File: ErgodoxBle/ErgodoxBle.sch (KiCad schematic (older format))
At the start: 90 parts, among them SW0:10 SW0:3, SW0:11 SW0:2, SW0:12 SW0:1, SW0:7 SW0:6, SW0:8 SW0:5, SW0:9 SW0:4, SW1:10 SW1:3, SW1:11 SW1:2, SW1:12 SW1:1, SW1:13 SW1:0, SW1:9 SW1:4, SW2:10 SW2:3, SW2:11 SW2:2, SW2:12 SW2:1, SW2:13 SW2:0, SW2:7 SW2:6, SW2:8 SW2:5, SW2:9 SW2:4, SW3:10 SW3:3, SW3:11 SW3:2, SW3:12 SW3:1, SW3:13 SW3:0, SW3:8 SW3:5, SW3:9 SW3:4, SW4:10 SW4:3, SW4:11 SW4:2, SW4:12 SW4:1, SW4:13 SW4:0, SW4:7 SW4:6, SW4:8 SW4:5, SW4:9 SW4:4, SW5:10 SW5:3, SW5:11 SW5:2, SW5:12 SW5:1, SW5:13 SW5:0, SW5:7 SW5:6, SW5:8 SW5:5, SW5:9 SW5:4

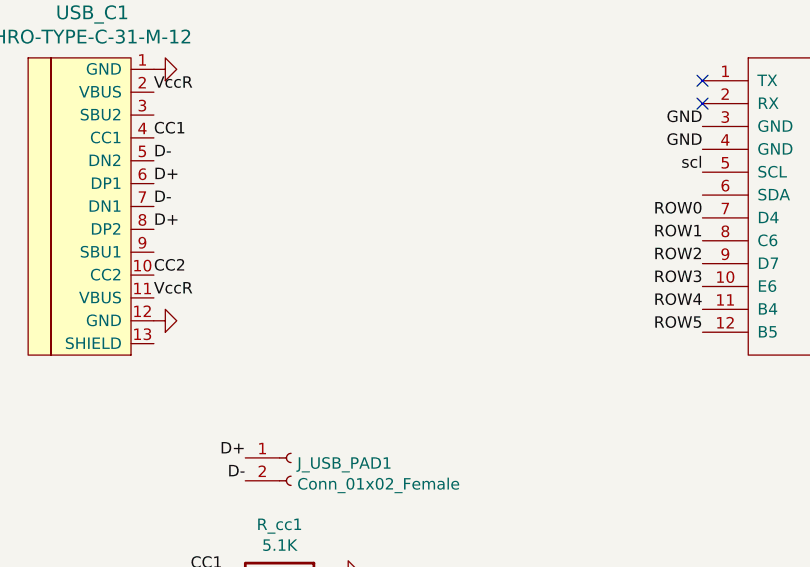
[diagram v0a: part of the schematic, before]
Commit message: Added pad for CR2032 module for bluemicro
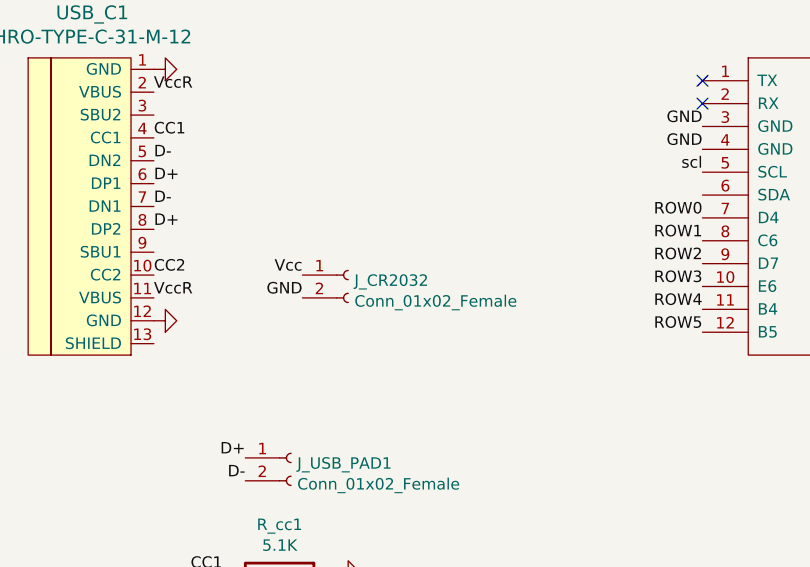
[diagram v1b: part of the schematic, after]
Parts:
- added J_CR2032: Conn_01x02_Female, Connector_Wire:SolderWirePad_1x02_P3.81mm_Drill0.8mm, symbol Connector:Conn_01x02_Female
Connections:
- net GND: now also J_CR2032.2 (Pin_2)
- net Vcc: now also J_CR2032.1 (Pin_1)
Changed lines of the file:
@@
 	1    0    0    -1
 $EndComp
+$Comp
+L Connector:Conn_01x02_Female J_CR2032
+U 1 1 5CA168E4
+P 2200 3200
+F 0 "J_CR2032" H 2227 3176 50  0000 L CNN
+F 1 "Conn_01x02_Female" H 2227 3085 50  0000 L CNN
+F 2 "Connector_Wire:SolderWirePad_1x02_P3.81mm_Drill0.8mm" H 2200 3200 50  0001 C CNN
+F 3 "~" H 2200 3200 50  0001 C CNN
+	1    2200 3200
+	1    0    0    -1
+$EndComp
+Text Label 2000 3200 2    50   ~ 0
+Vcc
+Text Label 2000 3300 2    50   ~ 0
+GND
 $EndSCHEMATC

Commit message: v 1.3, almost the final version
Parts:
- removed J_USB_PAD1: Conn_01x02_Female, Connector_Wire:SolderWirePad_1x02_P3.81mm_Drill0.8mm, symbol Connector:Conn_01x02_Female
- removed U_VR_IC1: AMS1117-3.3, Package_TO_SOT_SMD:SOT-223-3_TabPin2, symbol Regulator_Linear:AMS1117-3.3
- added D_RAW1, D_USB_HEADER1: D, Keebio-Parts:Diode-dual, symbol keyboard_parts:D
- added J_usb_break1: Conn_01x04_Female, Connector_Wire:SolderWirePad_1x04_P3.81mm_Drill1mm, symbol Connector:Conn_01x04_Female
- added U_ESD1: USBLC6-2SC6, Package_TO_SOT_SMD:SOT-23-6, symbol Power_Protection:USBLC6-2SC6
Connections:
- net D+: now also J_usb_break1.2 (Pin_2), U_ESD1.1 (IO1); no longer USB_C1.6 (DP1), USB_C1.8 (DP2)
- net D-: now also J_usb_break1.3 (Pin_3), U_ESD1.3 (IO2); no longer USB_C1.5 (DN2), USB_C1.7 (DN1)
- net GND: now also U_ESD1.2 (GND); no longer USB_C1.1 (GND), USB_C1.12 (GND), proMicro1.23 (GND)
- net VccR: now also D_RAW1.2, D_USB_HEADER1.2, U_ESD1.5 (VBUS)
- net VccRaw: now reaches proMicro1.24 (RAW)
- net VccRaw: now also D_RAW1.1
- new net D_IN+: USB_C1.6 (DP1), USB_C1.8 (DP2), U_ESD1.6 (IO1)
- new net D_IN-: USB_C1.5 (DN2), USB_C1.7 (DN1), U_ESD1.4 (IO2)
- new net GND_USB: J_usb_break1.4 (Pin_4), USB_C1.1 (GND), USB_C1.12 (GND), proMicro1.23 (GND)
- new net VUSB: D_USB_HEADER1.1, J_usb_break1.1 (Pin_1)
- no-connect marks 4 -> 3
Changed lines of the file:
@@
 	1    0    0    -1
 $EndComp
-$Comp
-L Connector:Conn_01x02_Female J_USB_PAD1
-U 1 1 5C943493
-P 1950 4000
-F 0 "J_USB_PAD1" H 1977 3976 50  0000 L CNN
-F 1 "Conn_01x02_Female" H 1977 3885 50  0000 L CNN
-F 2 "Connector_Wire:SolderWirePad_1x02_P3.81mm_Drill0.8mm" H 1950 4000 50  0001 C CNN
-F 3 "~" H 1950 4000 50  0001 C CNN
-	1    1950 4000
-	1    0    0    -1
-$EndComp
-Text Label 1750 4000 2    50   ~ 0
+Text Label 3300 4000 2    50   ~ 0
 D+
-Text Label 1750 4100 2    50   ~ 0
+Text Label 3300 4100 2    50   ~ 0
 D-
 $Comp
@@
 	0    -1   -1   0
 $EndComp
-Text Label 5150 2650 0    50   ~ 0
-Vcc
 Text Label 5150 2450 0    50   ~ 0
-GND
+GND_USB
 Text Label 3750 2550 2    50   ~ 0
 GND
@@
 NoConn ~ 3750 2350
 NoConn ~ 3750 2450
-NoConn ~ 5150 2350
 NoConn ~ 5150 2550
 $Comp
@@
 	1    0    0    -1
 $EndComp
-$Comp
-L component:GND #PWR0103
-U 1 1 5C6354D1
-P 1400 2300
-F 0 "#PWR0103" H 1400 2300 30  0001 C CNN
-F 1 "GND" H 1400 2230 30  0001 C CNN
-F 2 "" H 1400 2300 50  0001 C CNN
-F 3 "" H 1400 2300 50  0001 C CNN
-	1    1400 2300
-	0    -1   -1   0
-$EndComp
 Text Label 1350 2400 0    50   ~ 0
 VccR
@@
 Text Label 1350 3200 0    50   ~ 0
 CC2
-$Comp
-L component:GND #PWR0104
-U 1 1 5C646282
-P 1400 3400
-F 0 "#PWR0104" H 1400 3400 30  0001 C CNN
-F 1 "GND" H 1400 3330 30  0001 C CNN
-F 2 "" H 1400 3400 50  0001 C CNN
-F 3 "" H 1400 3400 50  0001 C CNN
-	1    1400 3400
-	0    -1   -1   0
-$EndComp
 Text Label 1350 3300 0    50   ~ 0
 VccR
 Text Label 1350 2700 0    50   ~ 0
-D-
+D_IN-
 Text Label 1350 2800 0    50   ~ 0
-D+
+D_IN+
 Text Label 1350 2900 0    50   ~ 0
-D-
+D_IN-
 Text Label 1350 3000 0    50   ~ 0
-D+
-$Comp
-L Regulator_Linear:AMS1117-3.3 U_VR_IC1
-U 1 1 5C499923
-P 2050 1400
-F 0 "U_VR_IC1" H 2050 1642 50  0000 C CNN
-F 1 "AMS1117-3.3" H 2050 1551 50  0000 C CNN
-F 2 "Package_TO_SOT_SMD:SOT-223-3_TabPin2" H 2050 1600 50  0001 C CNN
-F 3 "http://www.advanced-monolithic.com/pdf/ds1117.pdf" H 2150 1150 50  0001 C CNN
-	1    2050 1400
-	1    0    0    -1
-$EndComp
-Text Label 1750 1400 2    50   ~ 0
-VccR
-Text Label 2350 1400 0    50   ~ 0
-Vcc
-$Comp
-L component:GND #PWR0105
-U 1 1 5C49AE71
-P 2050 1750
-F 0 "#PWR0105" H 2050 1750 30  0001 C CNN
-F 1 "GND" H 2050 1680 30  0001 C CNN
-F 2 "" H 2050 1750 50  0001 C CNN
-F 3 "" H 2050 1750 50  0001 C CNN
-	1    2050 1750
-	1    0    0    -1
-$EndComp
+D_IN+
 $Comp
 L Connector:Conn_01x02_Female J_CR2032
@@
 Text Label 2000 3300 2    50   ~ 0
 GND
+$Comp
+L keyboard_parts:D D_RAW1
+U 1 1 5CBC3CF1
+P 2100 1250
+F 0 "D_RAW1" V 1919 1200 60  0000 C CNN
+F 1 "D" V 2250 1200 60  0001 C CNN
+F 2 "Keebio-Parts:Diode-dual" H 2100 1250 60  0001 C CNN
+F 3 "" H 2100 1250 60  0000 C CNN
+	1    2100 1250
+	0    1    1    0
+$EndComp
+$Comp
+L keyboard_parts:D D_USB_HEADER1
+U 1 1 5CBC3EC6
+P 2100 1600
+F 0 "D_USB_HEADER1" V 1919 1550 60  0000 C CNN
+F 1 "D" V 2250 1550 60  0001 C CNN
+F 2 "Keebio-Parts:Diode-dual" H 2100 1600 60  0001 C CNN
+F 3 "" H 2100 1600 60  0000 C CNN
+	1    2100 1600
+	0    1    1    0
+$EndComp
+Text Label 1950 1250 2    50   ~ 0
+VccR
+Text Label 1950 1600 2    50   ~ 0
+VccR
+Text Label 2150 1250 0    50   ~ 0
+VccRaw
+Text Label 2150 1600 0    50   ~ 0
+VUSB
+Text Label 5150 2350 0    50   ~ 0
+VccRaw
+Text Label 1350 2300 0    50   ~ 0
+GND_USB
+Text Label 1350 3400 0    50   ~ 0
+GND_USB
+Text Label 3300 3900 2    50   ~ 0
+VUSB
+Text Label 3300 4200 2    50   ~ 0
+GND_USB
+Text Label 5150 2650 0    50   ~ 0
+Vcc
+$Comp
+L Power_Protection:USBLC6-2SC6 U_ESD1
+U 1 1 5CBD2D52
+P 3450 1450
+F 0 "U_ESD1" H 3450 2128 50  0000 C CNN
+F 1 "USBLC6-2SC6" H 3450 2037 50  0000 C CNN
+F 2 "Package_TO_SOT_SMD:SOT-23-6" H 2700 1850 50  0001 C CNN
+F 3 "http://www2.st.com/resource/en/datasheet/CD00050750.pdf" H 3650 1800 50  0001 C CNN
+	1    3450 1450
+	1    0    0    -1
+$EndComp
+Text Label 3450 950  0    50   ~ 0
+VccR
+Text Label 2950 1350 2    50   ~ 0
+D_IN+
+Text Label 3950 1350 0    50   ~ 0
+D_IN-
+Text Label 2950 1550 2    50   ~ 0
+D+
+Text Label 3950 1550 0    50   ~ 0
+D-
+$Comp
+L component:GND #PWR0103
+U 1 1 5CBD3635
+P 3450 2000
+F 0 "#PWR0103" H 3450 2000 30  0001 C CNN
+F 1 "GND" H 3450 1930 30  0001 C CNN
+F 2 "" H 3450 2000 50  0001 C CNN
+F 3 "" H 3450 2000 50  0001 C CNN
+	1    3450 2000
+	1    0    0    -1
+$EndComp
+$Comp
+L Connector:Conn_01x04_Female J_usb_break1
+U 1 1 5CC50D9F
+P 3500 4000
+F 0 "J_usb_break1" H 3527 3976 50  0000 L CNN
+F 1 "Conn_01x04_Female" H 3527 3885 50  0000 L CNN
+F 2 "Connector_Wire:SolderWirePad_1x04_P3.81mm_Drill1mm" H 3500 4000 50  0001 C CNN
+F 3 "~" H 3500 4000 50  0001 C CNN
+	1    3500 4000
+	1    0    0    -1
+$EndComp
 $EndSCHEMATC

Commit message: final version before hardware testing
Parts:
- added USB_C2: HRO-TYPE-C-31-M-12, usbc_footprint:HRO-TYPE-C-31-M-12, symbol Type-C:HRO-TYPE-C-31-M-12
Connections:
- net CC1: now also USB_C2.4 (CC1)
- net CC2: now also USB_C2.10 (CC2)
- net D_IN+: now also USB_C2.6 (DP1), USB_C2.8 (DP2)
- net D_IN-: now also USB_C2.5 (DN2), USB_C2.7 (DN1)
- net GND_USB: now also USB_C2.1 (GND), USB_C2.12 (GND)
- net VccR: now also USB_C2.11 (VBUS), USB_C2.2 (VBUS)
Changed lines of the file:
@@
 	1    0    0    -1
 $EndComp
+$Comp
+L Type-C:HRO-TYPE-C-31-M-12 USB_C2
+U 1 1 5CC80FFB
+P 6450 1700
+F 0 "USB_C2" H 6281 2497 60  0000 C CNN
+F 1 "HRO-TYPE-C-31-M-12" H 6281 2391 60  0000 C CNN
+F 2 "usbc_footprint:HRO-TYPE-C-31-M-12" H 6450 1700 60  0001 C CNN
+F 3 "" H 6450 1700 60  0001 C CNN
+	1    6450 1700
+	1    0    0    -1
+$EndComp
+Text Label 6550 1250 0    50   ~ 0
+VccR
+Text Label 6550 1450 0    50   ~ 0
+CC1
+Text Label 6550 2050 0    50   ~ 0
+CC2
+Text Label 6550 2150 0    50   ~ 0
+VccR
+Text Label 6550 1550 0    50   ~ 0
+D_IN-
+Text Label 6550 1650 0    50   ~ 0
+D_IN+
+Text Label 6550 1750 0    50   ~ 0
+D_IN-
+Text Label 6550 1850 0    50   ~ 0
+D_IN+
+Text Label 6550 1150 0    50   ~ 0
+GND_USB
+Text Label 6550 2250 0    50   ~ 0
+GND_USB
 $EndSCHEMATC

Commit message: minor changes
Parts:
- removed D_RAW1, D_USB_HEADER1: D, Keebio-Parts:Diode-dual, symbol keyboard_parts:D
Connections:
- net VccR is gone; now on net VUSB: USB_C1.11 (VBUS), USB_C1.2 (VBUS), USB_C2.11 (VBUS), USB_C2.2 (VBUS), U_ESD1.5 (VBUS)
- net GND_USB: no longer proMicro1.23 (GND)
- net VccRaw: no longer names the net of proMicro1.24 (RAW)
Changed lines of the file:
@@
 	0    -1   -1   0
 $EndComp
-Text Label 5150 2450 0    50   ~ 0
-GND_USB
 Text Label 3750 2550 2    50   ~ 0
 GND
@@
 $EndComp
 Text Label 1350 2400 0    50   ~ 0
-VccR
+VUSB
 Text Label 1350 2600 0    50   ~ 0
 CC1
@@
 CC2
 Text Label 1350 3300 0    50   ~ 0
-VccR
+VUSB
 Text Label 1350 2700 0    50   ~ 0
 D_IN-
@@
 Text Label 2000 3300 2    50   ~ 0
 GND
-$Comp
-L keyboard_parts:D D_RAW1
-U 1 1 5CBC3CF1
-P 2100 1250
-F 0 "D_RAW1" V 1919 1200 60  0000 C CNN
-F 1 "D" V 2250 1200 60  0001 C CNN
-F 2 "Keebio-Parts:Diode-dual" H 2100 1250 60  0001 C CNN
-F 3 "" H 2100 1250 60  0000 C CNN
-	1    2100 1250
-	0    1    1    0
-$EndComp
-$Comp
-L keyboard_parts:D D_USB_HEADER1
-U 1 1 5CBC3EC6
-P 2100 1600
-F 0 "D_USB_HEADER1" V 1919 1550 60  0000 C CNN
-F 1 "D" V 2250 1550 60  0001 C CNN
-F 2 "Keebio-Parts:Diode-dual" H 2100 1600 60  0001 C CNN
-F 3 "" H 2100 1600 60  0000 C CNN
-	1    2100 1600
-	0    1    1    0
-$EndComp
-Text Label 1950 1250 2    50   ~ 0
-VccR
-Text Label 1950 1600 2    50   ~ 0
-VccR
-Text Label 2150 1250 0    50   ~ 0
-VccRaw
-Text Label 2150 1600 0    50   ~ 0
-VUSB
-Text Label 5150 2350 0    50   ~ 0
-VccRaw
 Text Label 1350 2300 0    50   ~ 0
 GND_USB
@@
 $EndComp
 Text Label 3450 950  0    50   ~ 0
-VccR
+VUSB
 Text Label 2950 1350 2    50   ~ 0
 D_IN+
@@
 $EndComp
 Text Label 6550 1250 0    50   ~ 0
-VccR
+VUSB
 Text Label 6550 1450 0    50   ~ 0
 CC1
@@
 CC2
 Text Label 6550 2150 0    50   ~ 0
-VccR
+VUSB
 Text Label 6550 1550 0    50   ~ 0
 D_IN-

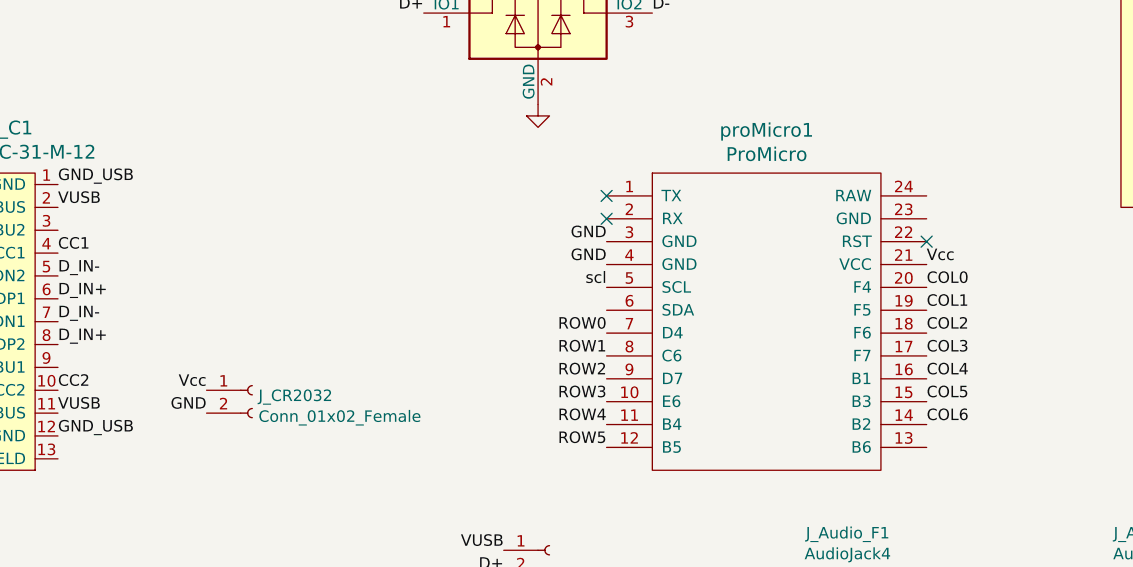
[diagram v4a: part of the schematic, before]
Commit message: added svg for case
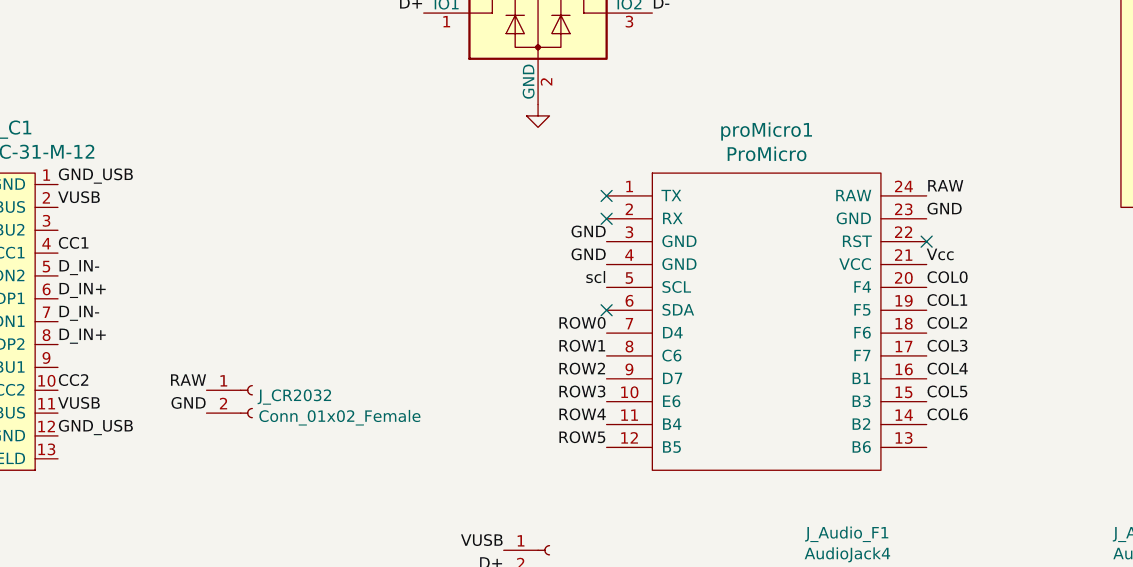
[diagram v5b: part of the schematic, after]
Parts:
- J_CR2032: footprint Connector_Wire:SolderWirePad_1x02_P3.81mm_Drill0.8mm -> usbc_footprint:Custom_SolderWirePad_1x02_P1.75mm_Drill1.09mm
- J_usb_break1: footprint Connector_Wire:SolderWirePad_1x04_P3.81mm_Drill1mm -> usbc_footprint:Custom_SolderWirePad_1x04_P1.7526mm_Drill1.0922mm
- SW0:10, SW0:11: footprint Keebio-Parts:Hybrid_PCB_100H_Dual_hole -> Keebio-Parts:Hybrid_PCB_200H-dual
- SW2:13, SW3:13, SW4:13, SW5:13: footprint Keebio-Parts:Hybrid_PCB_100H_Dual_hole -> usbc_footprint:correct_Hybrid_PCB_100v_150H_Dual_hole
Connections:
- net GND: now also proMicro1.23 (GND)
- net Vcc: no longer J_CR2032.1 (Pin_1)
- net RAW: now reaches proMicro1.24 (RAW)
- net RAW: now also J_CR2032.1 (Pin_1)
- no-connect marks 3 -> 4
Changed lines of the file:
@@
 F 0 "SW0:11" H 4850 9410 50  0000 C CNN
 F 1 "SW0:2" H 4700 9220 50  0000 C CNN
-F 2 "Keebio-Parts:Hybrid_PCB_100H_Dual_hole" H 4700 9300 60  0001 C CNN
+F 2 "Keebio-Parts:Hybrid_PCB_200H-dual" H 4700 9300 60  0001 C CNN
 F 3 "" H 4700 9300 60  0001 C CNN
 	1    4700 9300
@@
 F 0 "SW2:13" H 6250 8110 50  0000 C CNN
 F 1 "SW2:0" H 6100 7920 50  0000 C CNN
-F 2 "Keebio-Parts:Hybrid_PCB_100H_Dual_hole" H 6100 8000 60  0001 C CNN
+F 2 "usbc_footprint:correct_Hybrid_PCB_100v_150H_Dual_hole" H 6100 8000 60  0001 C CNN
 F 3 "" H 6100 8000 60  0001 C CNN
 	1    6100 8000
@@
 F 0 "SW3:13" H 6250 7460 50  0000 C CNN
 F 1 "SW3:0" H 6100 7270 50  0000 C CNN
-F 2 "Keebio-Parts:Hybrid_PCB_100H_Dual_hole" H 6100 7350 60  0001 C CNN
+F 2 "usbc_footprint:correct_Hybrid_PCB_100v_150H_Dual_hole" H 6100 7350 60  0001 C CNN
 F 3 "" H 6100 7350 60  0001 C CNN
 	1    6100 7350
@@
 F 0 "SW4:13" H 6250 6810 50  0000 C CNN
 F 1 "SW4:0" H 6100 6620 50  0000 C CNN
-F 2 "Keebio-Parts:Hybrid_PCB_100H_Dual_hole" H 6100 6700 60  0001 C CNN
+F 2 "usbc_footprint:correct_Hybrid_PCB_100v_150H_Dual_hole" H 6100 6700 60  0001 C CNN
 F 3 "" H 6100 6700 60  0001 C CNN
 	1    6100 6700
@@
 F 0 "SW5:13" H 6250 6160 50  0000 C CNN
 F 1 "SW5:0" H 6100 5970 50  0000 C CNN
-F 2 "Keebio-Parts:Hybrid_PCB_100H_Dual_hole" H 6100 6050 60  0001 C CNN
+F 2 "usbc_footprint:correct_Hybrid_PCB_100v_150H_Dual_hole" H 6100 6050 60  0001 C CNN
 F 3 "" H 6100 6050 60  0001 C CNN
 	1    6100 6050
@@
 F 0 "SW0:10" H 4150 9410 50  0000 C CNN
 F 1 "SW0:3" H 4000 9220 50  0000 C CNN
-F 2 "Keebio-Parts:Hybrid_PCB_100H_Dual_hole" H 4000 9300 60  0001 C CNN
+F 2 "Keebio-Parts:Hybrid_PCB_200H-dual" H 4000 9300 60  0001 C CNN
 F 3 "" H 4000 9300 60  0001 C CNN
 	1    4000 9300
@@
 F 0 "J_CR2032" H 2227 3176 50  0000 L CNN
 F 1 "Conn_01x02_Female" H 2227 3085 50  0000 L CNN
-F 2 "Connector_Wire:SolderWirePad_1x02_P3.81mm_Drill0.8mm" H 2200 3200 50  0001 C CNN
+F 2 "usbc_footprint:Custom_SolderWirePad_1x02_P1.75mm_Drill1.09mm" H 2200 3200 50  0001 C CNN
 F 3 "~" H 2200 3200 50  0001 C CNN
 	1    2200 3200
@@
 $EndComp
 Text Label 2000 3200 2    50   ~ 0
-Vcc
+RAW
 Text Label 2000 3300 2    50   ~ 0
 GND
@@
 F 0 "J_usb_break1" H 3527 3976 50  0000 L CNN
 F 1 "Conn_01x04_Female" H 3527 3885 50  0000 L CNN
-F 2 "Connector_Wire:SolderWirePad_1x04_P3.81mm_Drill1mm" H 3500 4000 50  0001 C CNN
+F 2 "usbc_footprint:Custom_SolderWirePad_1x04_P1.7526mm_Drill1.0922mm" H 3500 4000 50  0001 C CNN
 F 3 "~" H 3500 4000 50  0001 C CNN
 	1    3500 4000
@@
 Text Label 6550 2250 0    50   ~ 0
 GND_USB
+Text Label 5150 2350 0    50   ~ 0
+RAW
+Text Label 5150 2450 0    50   ~ 0
+GND
+NoConn ~ 3750 2850
 $EndSCHEMATC
